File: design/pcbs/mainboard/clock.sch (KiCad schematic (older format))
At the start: 8 parts, among them U15 CCHD-575, U16 5PB1102

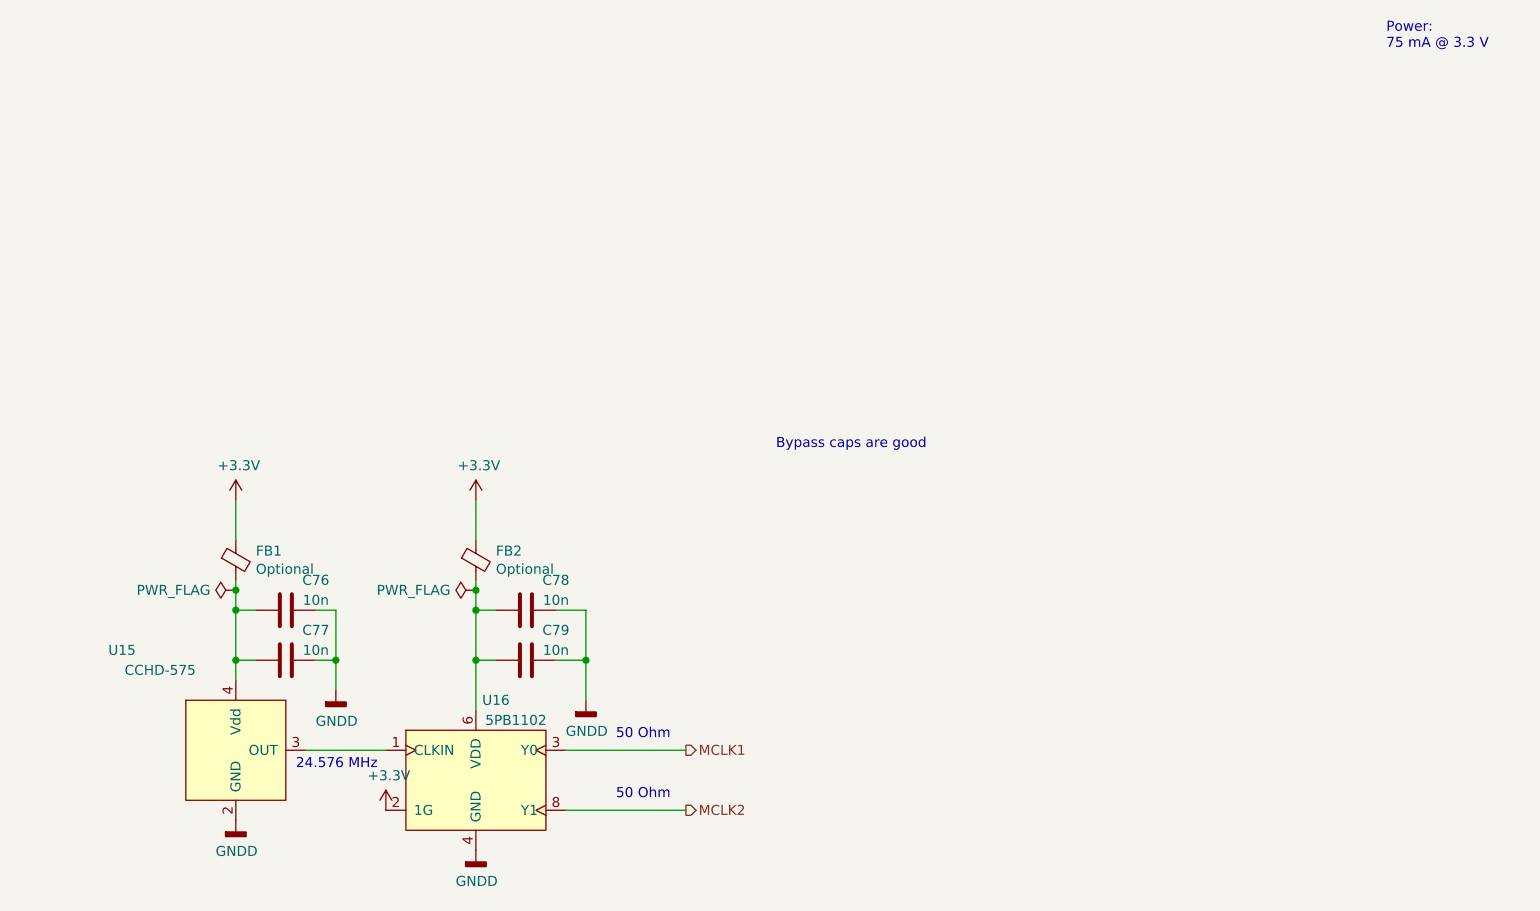
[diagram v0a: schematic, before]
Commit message: Completed layout of main board, cleaned up some libraries.
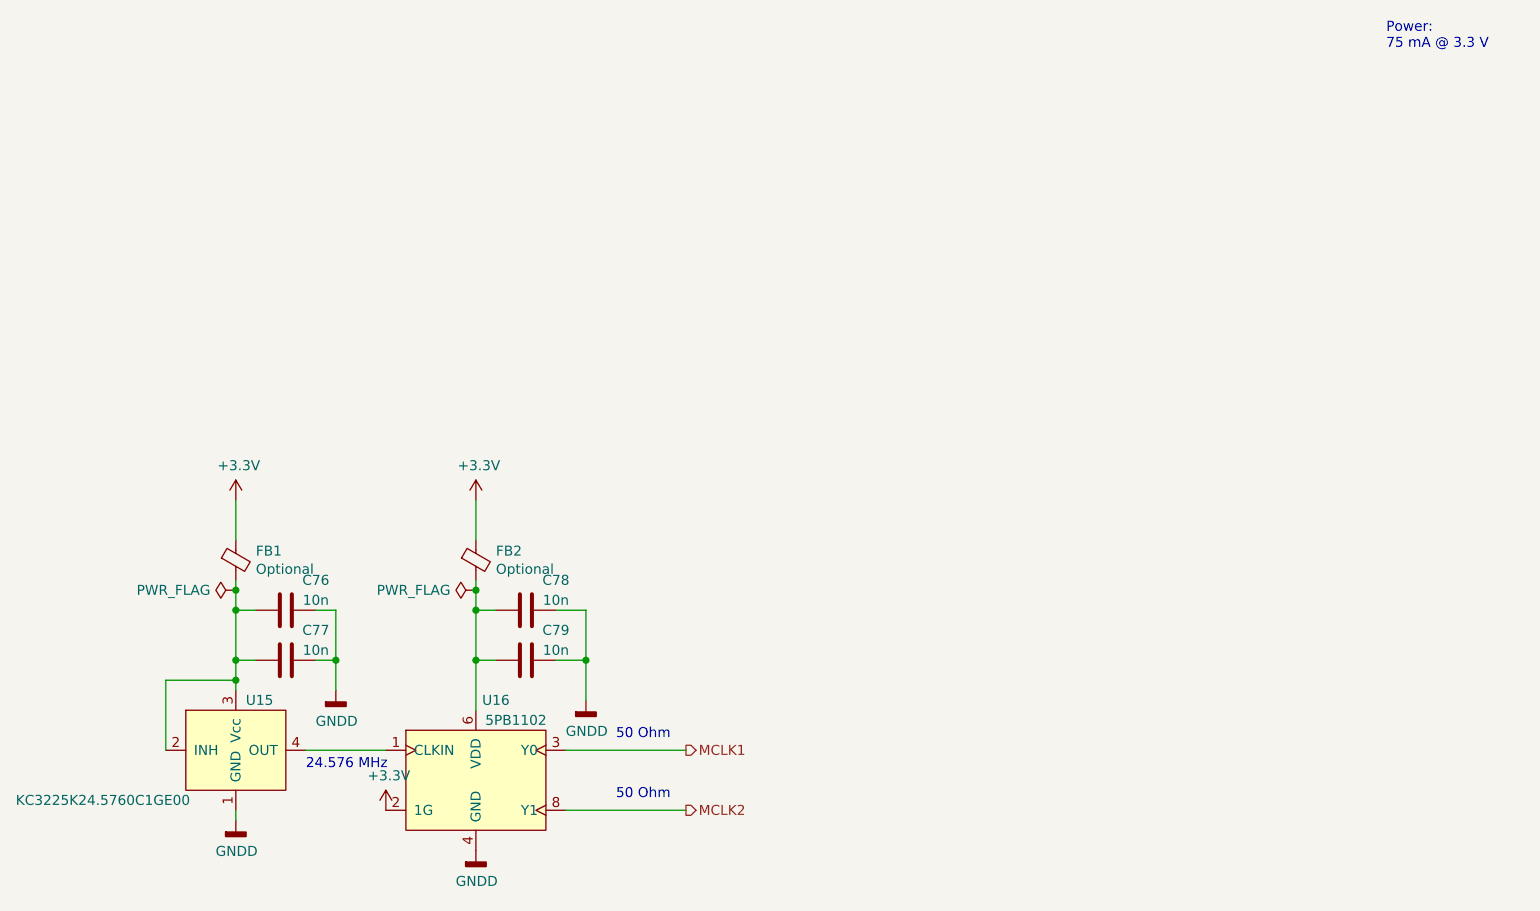
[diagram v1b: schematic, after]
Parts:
- removed U15: CCHD-575, mainboard:CCHD-575, symbol dac:CCHD-575
- added U15: KC3225K24.5760C1GE00, Crystal:Crystal_SMD_3225-4Pin_3.2x2.5mm, symbol dac:KC3225K24.5760C1GE00
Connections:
- net GNDD: now also U15.1 (GND)
- net at U16.1 (CLKIN): now also U15.4 (OUT)
- net at C76.2, C77.2, FB1.2: now also U15.2 (INH), U15.3 (Vcc)
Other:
- note removed: "Bypass caps are good"
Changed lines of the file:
@@
 MCLK1
-$Comp
-L dac:CCHD-575 U15
-U 1 1 5ECD281C
-P 4750 4250
-F 0 "U15" H 4250 4750 50  0000 R CNN
-F 1 "CCHD-575" H 4550 4650 50  0000 R CNN
-F 2 "mainboard:CCHD-575" H 4750 4250 50  0001 C CNN
-F 3 "https://www.crystek.com/crystal/spec-sheets/clock/CCHD-575.pdf" H 4750 4250 50  0001 C CNN
-F 4 "744-1747-ND" H 4750 4250 50  0001 C CNN "DigiKey"
-F 5 "Yes" H 4750 4250 50  0001 C CNN "Done"
-	1    4750 4250
-	1    0    0    -1
-$EndComp
 $Comp
 L Device:C C77
@@
 	4850 3800 4750 3800
 Wire Wire Line
-	4750 3800 4750 3900
-Wire Wire Line
 	5150 3800 5250 3800
 Wire Wire Line
@@
 Wire Wire Line
 	5500 4250 5100 4250
-Text Notes 5050 4350 0    50   ~ 0
+Text Notes 5100 4350 0    50   ~ 0
 24.576 MHz
 $Comp
@@
 Wire Wire Line
 	5950 3400 5950 3450
-Text Notes 7450 2750 0    50   ~ 0
-Bypass caps are good
 $Comp
 L Device:C C76
@@
 	1    0    0    -1
 $EndComp
+$Comp
+L dac:KC3225K24.5760C1GE00 U15
+U 1 1 5EF5DFBA
+P 4750 4250
+F 0 "U15" H 4800 4500 50  0000 L CNN
+F 1 "KC3225K24.5760C1GE00" H 3650 4000 50  0000 L CNN
+F 2 "Crystal:Crystal_SMD_3225-4Pin_3.2x2.5mm" H 4750 3800 50  0001 C CNN
+F 3 "http://global.kyocera.com/prdct/electro/product/pdf/clock_k_e.pdf" H 4750 4250 50  0001 C CNN
+F 4 "1253-1407-1-ND" H 5144 4159 50  0001 L CNN "DigiKey"
+	1    4750 4250
+	1    0    0    -1
+$EndComp
+Wire Wire Line
+	4750 3800 4750 3900
+Wire Wire Line
+	4750 4550 4750 4600
+Wire Wire Line
+	4400 4250 4400 3900
+Wire Wire Line
+	4400 3900 4750 3900
+Connection ~ 4750 3900
+Wire Wire Line
+	4750 3900 4750 3950
 $EndSCHEMATC

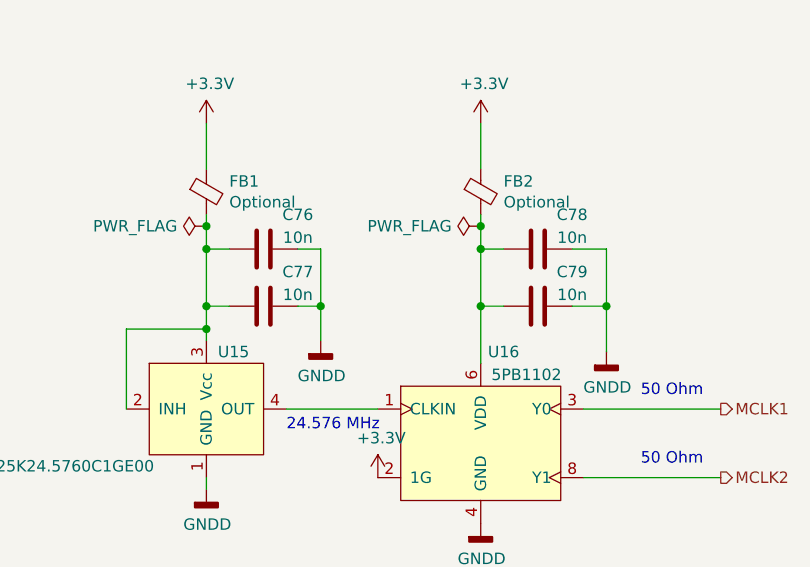
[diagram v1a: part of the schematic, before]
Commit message: Renumbered footprints to follow board position.
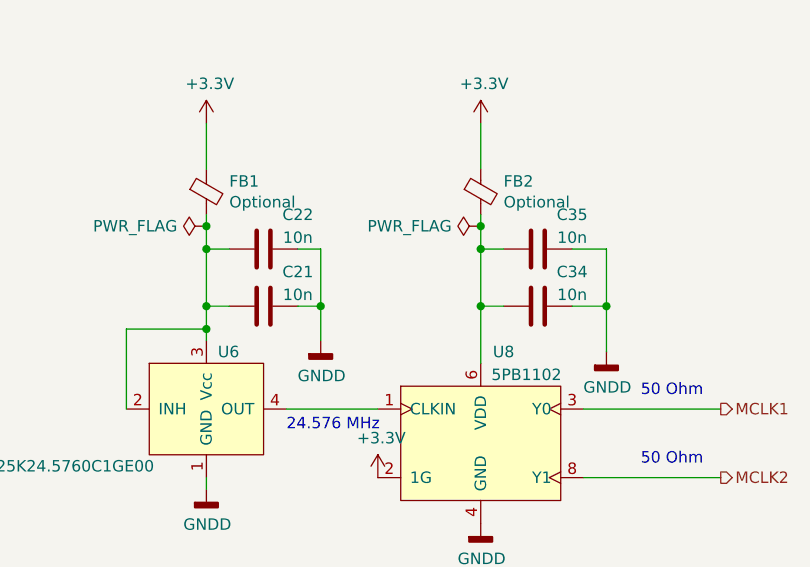
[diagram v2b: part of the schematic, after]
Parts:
- renumbered C77 to C21, C76 to C22, C79 to C34, C78 to C35, U15 to U6, U16 to U8
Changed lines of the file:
@@
 MCLK1
 $Comp
-L Device:C C77
+L Device:C C21
 U 1 1 5ECD2BD1
 P 5000 3800
-F 0 "C77" V 4850 3950 50  0000 C CNN
+F 0 "C21" V 4850 3950 50  0000 C CNN
 F 1 "10n" V 4950 3950 50  0000 C CNN
 F 2 "Capacitor_SMD:C_0603_1608Metric" H 5038 3650 50  0001 C CNN
@@
 	4750 3400 4750 3450
 $Comp
-L dac:5PB1102 U16
+L dac:5PB1102 U8
 U 1 1 5ECAB577
 P 5950 4400
-F 0 "U16" H 6050 4800 50  0000 C CNN
+F 0 "U8" H 6050 4800 50  0000 C CNN
 F 1 "5PB1102" H 6150 4700 50  0000 C CNN
 F 2 "Package_SO:TSSOP-8_4.4x3mm_P0.65mm" H 6100 4150 50  0001 C CNN
@@
 $EndComp
 $Comp
-L Device:C C79
+L Device:C C34
 U 1 1 5ECAEA63
 P 6200 3800
-F 0 "C79" V 6050 3950 50  0000 C CNN
+F 0 "C34" V 6050 3950 50  0000 C CNN
 F 1 "10n" V 6150 3950 50  0000 C CNN
 F 2 "Capacitor_SMD:C_0603_1608Metric" H 6238 3650 50  0001 C CNN
@@
 	5950 3400 5950 3450
 $Comp
-L Device:C C76
+L Device:C C22
 U 1 1 5ECEC618
 P 5000 3550
-F 0 "C76" V 4850 3700 50  0000 C CNN
+F 0 "C22" V 4850 3700 50  0000 C CNN
 F 1 "10n" V 4950 3700 50  0000 C CNN
 F 2 "Capacitor_SMD:C_0603_1608Metric" H 5038 3400 50  0001 C CNN
@@
 Connection ~ 5250 3800
 $Comp
-L Device:C C78
+L Device:C C35
 U 1 1 5ECECE2D
 P 6200 3550
-F 0 "C78" V 6050 3700 50  0000 C CNN
+F 0 "C35" V 6050 3700 50  0000 C CNN
 F 1 "10n" V 6150 3700 50  0000 C CNN
 F 2 "Capacitor_SMD:C_0603_1608Metric" H 6238 3400 50  0001 C CNN
@@
 $EndComp
 $Comp
-L dac:KC3225K24.5760C1GE00 U15
+L dac:KC3225K24.5760C1GE00 U6
 U 1 1 5EF5DFBA
 P 4750 4250
-F 0 "U15" H 4800 4500 50  0000 L CNN
+F 0 "U6" H 4800 4500 50  0000 L CNN
 F 1 "KC3225K24.5760C1GE00" H 3650 4000 50  0000 L CNN
 F 2 "Crystal:Crystal_SMD_3225-4Pin_3.2x2.5mm" H 4750 3800 50  0001 C CNN

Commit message: Updated PCB sheet info. Clarified licence in readme.
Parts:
- U6: Done (none) -> Yes
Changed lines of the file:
@@
 F 3 "http://global.kyocera.com/prdct/electro/product/pdf/clock_k_e.pdf" H 4750 4250 50  0001 C CNN
 F 4 "1253-1407-1-ND" H 5144 4159 50  0001 L CNN "DigiKey"
+F 5 "Yes" H 4750 4250 50  0001 C CNN "Done"
 	1    4750 4250
 	1    0    0    -1

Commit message: Fixed title blocks. Added fab outputs.
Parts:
- U8: LCSC (none) -> C150285
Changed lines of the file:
@@
 encoding utf-8
 Sheet 8 10
-Title ""
-Date ""
-Rev ""
-Comp ""
-Comment1 ""
-Comment2 ""
+Title "DAC1 Main board"
+Date "2020-06-27"
+Rev "1.0.0"
+Comp "© Mark Pinese 2020"
+Comment1 "To view a copy of this license, visit https://creativecommons.org/licenses/by/4.0"
+Comment2 "This work is licensed under CC BY 4.0."
 Comment3 ""
 Comment4 ""
@@
 F 4 "800-2889-5-ND" H 5950 4400 50  0001 C CNN "DigiKey"
 F 5 "Yes" H 5950 4400 50  0001 C CNN "Done"
+F 6 "C150285" H 5950 4400 50  0001 C CNN "LCSC"
 	1    5950 4400
 	1    0    0    -1

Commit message: Misc updates
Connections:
- net GNDD renamed GND
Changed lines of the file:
@@
 	4750 3450 4750 3550
-$Comp
-L power:GNDD #PWR0116
-U 1 1 5F292F45
-P 4750 4600
-F 0 "#PWR0116" H 4750 4350 50  0001 C CNN
-F 1 "GNDD" H 4754 4445 50  0000 C CNN
-F 2 "" H 4750 4600 50  0001 C CNN
-F 3 "" H 4750 4600 50  0001 C CNN
-	1    4750 4600
-	1    0    0    -1
-$EndComp
-$Comp
-L power:GNDD #PWR0117
-U 1 1 5F293E89
-P 5250 3950
-F 0 "#PWR0117" H 5250 3700 50  0001 C CNN
-F 1 "GNDD" H 5254 3795 50  0000 C CNN
-F 2 "" H 5250 3950 50  0001 C CNN
-F 3 "" H 5250 3950 50  0001 C CNN
-	1    5250 3950
-	1    0    0    -1
-$EndComp
-$Comp
-L power:GNDD #PWR0118
-U 1 1 5F2941BE
-P 5950 4750
-F 0 "#PWR0118" H 5950 4500 50  0001 C CNN
-F 1 "GNDD" H 5954 4595 50  0000 C CNN
-F 2 "" H 5950 4750 50  0001 C CNN
-F 3 "" H 5950 4750 50  0001 C CNN
-	1    5950 4750
-	1    0    0    -1
-$EndComp
-$Comp
-L power:GNDD #PWR0119
-U 1 1 5F294768
-P 6500 4000
-F 0 "#PWR0119" H 6500 3750 50  0001 C CNN
-F 1 "GNDD" H 6504 3845 50  0000 C CNN
-F 2 "" H 6500 4000 50  0001 C CNN
-F 3 "" H 6500 4000 50  0001 C CNN
-	1    6500 4000
-	1    0    0    -1
-$EndComp
 $Comp
 L dac:KC3225K24.5760C1GE00 U6
@@
 Wire Wire Line
 	4750 3900 4750 3950
+$Comp
+L power:GND #PWR041
+U 1 1 5F004206
+P 4750 4600
+F 0 "#PWR041" H 4750 4350 50  0001 C CNN
+F 1 "GND" H 4755 4427 50  0000 C CNN
+F 2 "" H 4750 4600 50  0001 C CNN
+F 3 "" H 4750 4600 50  0001 C CNN
+	1    4750 4600
+	1    0    0    -1
+$EndComp
+$Comp
+L power:GND #PWR042
+U 1 1 5F004942
+P 5250 3950
+F 0 "#PWR042" H 5250 3700 50  0001 C CNN
+F 1 "GND" H 5255 3777 50  0000 C CNN
+F 2 "" H 5250 3950 50  0001 C CNN
+F 3 "" H 5250 3950 50  0001 C CNN
+	1    5250 3950
+	1    0    0    -1
+$EndComp
+$Comp
+L power:GND #PWR044
+U 1 1 5F004EB1
+P 6500 4000
+F 0 "#PWR044" H 6500 3750 50  0001 C CNN
+F 1 "GND" H 6505 3827 50  0000 C CNN
+F 2 "" H 6500 4000 50  0001 C CNN
+F 3 "" H 6500 4000 50  0001 C CNN
+	1    6500 4000
+	1    0    0    -1
+$EndComp
+$Comp
+L power:GND #PWR043
+U 1 1 5F0053DE
+P 5950 4750
+F 0 "#PWR043" H 5950 4500 50  0001 C CNN
+F 1 "GND" H 5955 4577 50  0000 C CNN
+F 2 "" H 5950 4750 50  0001 C CNN
+F 3 "" H 5950 4750 50  0001 C CNN
+	1    5950 4750
+	1    0    0    -1
+$EndComp
 $EndSCHEMATC
